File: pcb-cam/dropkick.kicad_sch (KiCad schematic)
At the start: 50 parts, among them J1 Conn_01x10, SW1 450405020524, SW2 KMR211NG_LFS, U1 SPX3819-3.3, U2 MCP73831T-2ACI/OT, U3 CAM-M8C-0, U4 ATSAMD21G18A-AUT, U5 DPS310XTSA1, U6 MPU-6050, X1 USB micro-B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

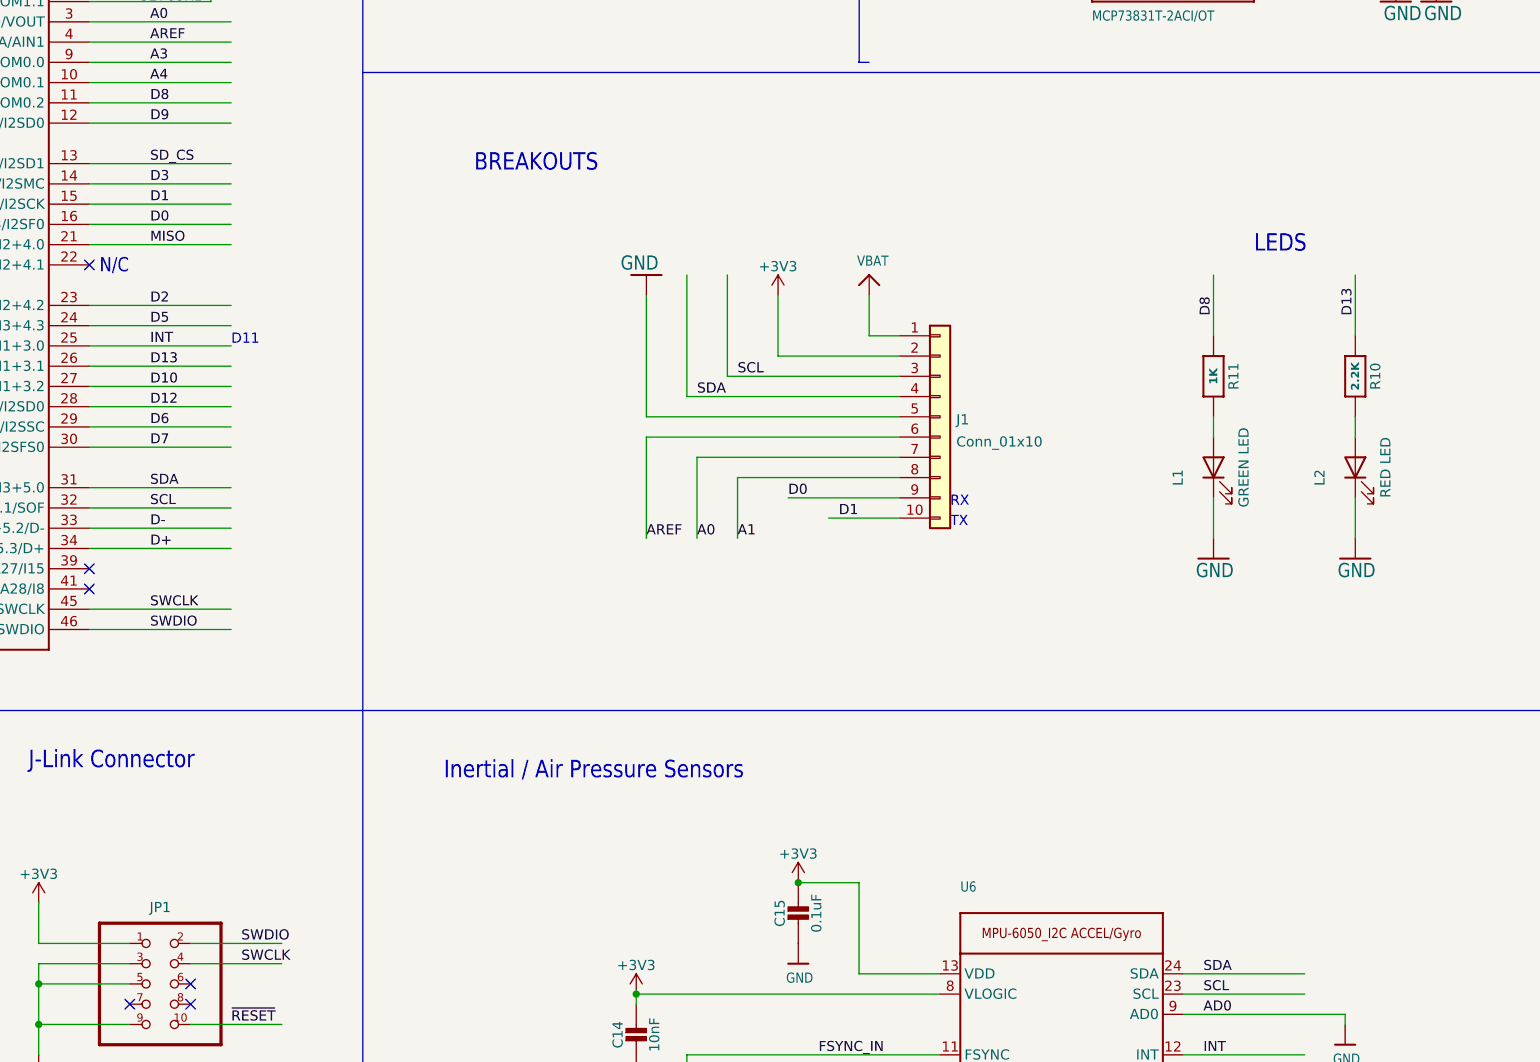
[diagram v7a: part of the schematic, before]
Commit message: Switch to 2.0mm pads and added SWDIO/SWCLK pads to flash w/o header
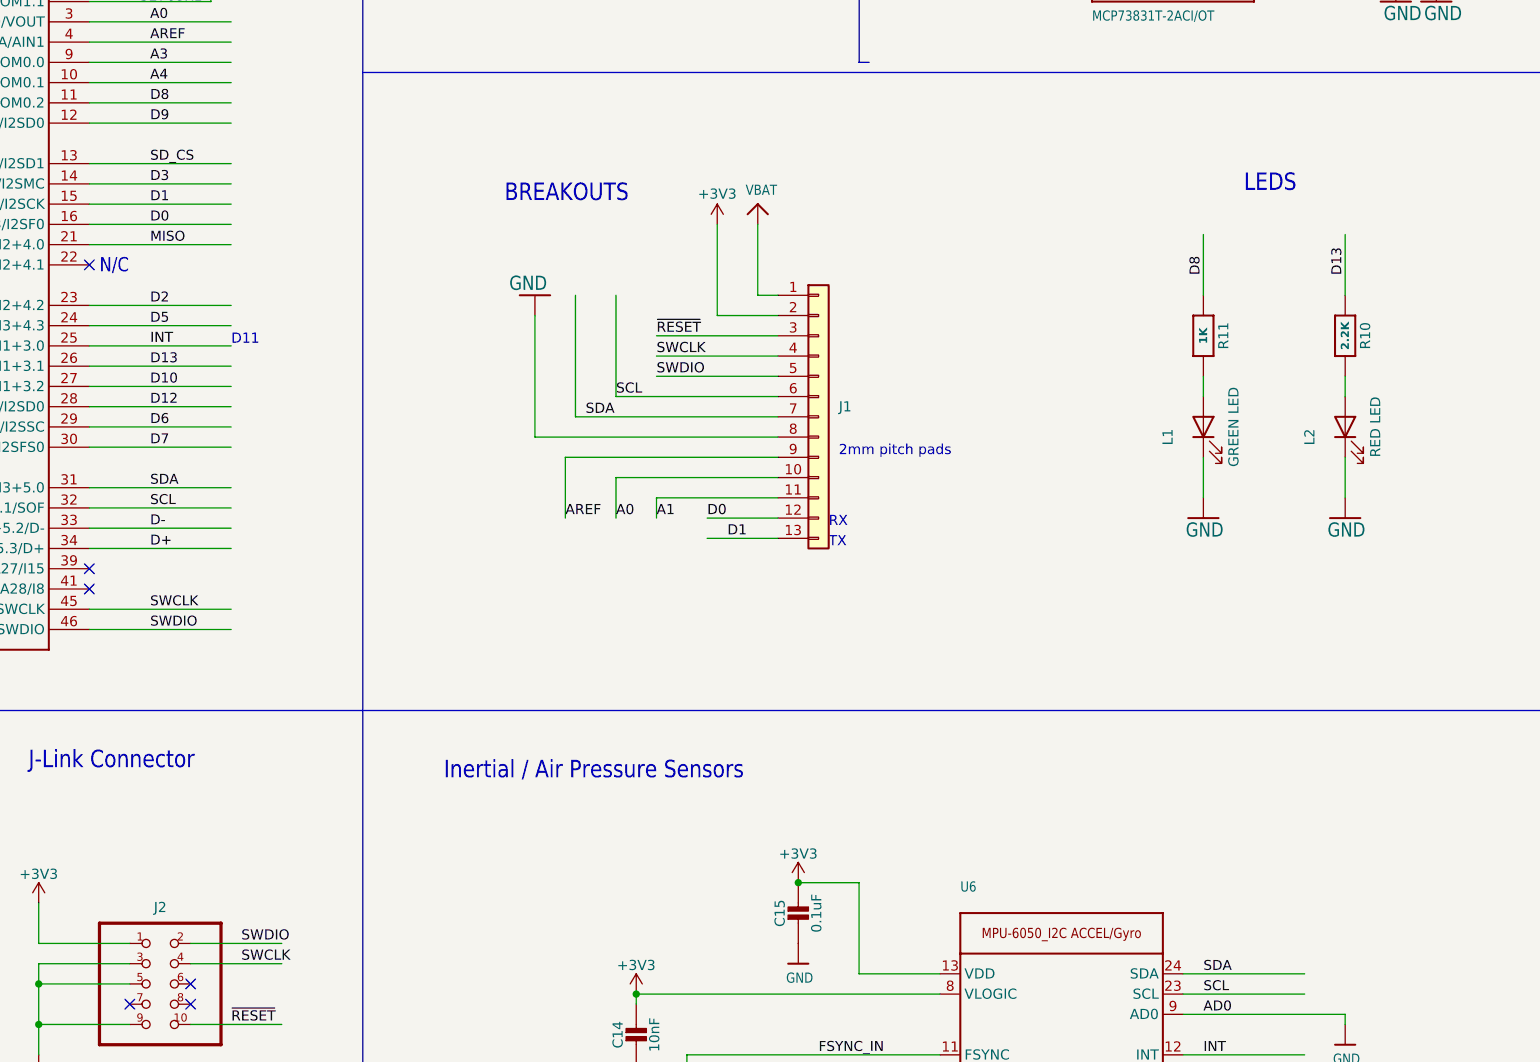
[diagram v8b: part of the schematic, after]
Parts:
- removed J1: Conn_01x10, Connector_PinSocket_2.54mm:PinSocket_1x10_P2.54mm_Vertical, symbol Connector_Generic:Conn_01x10
- added J1: Conn_01x13, Connector_PinSocket_2.00mm:PinSocket_1x13_P2.00mm_Vertical, symbol Connector_Generic:Conn_01x13
- R12, R13, R14, R4: Comments R11-R12 DNP -> (none)
- renumbered JP1 to J2
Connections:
- net +3V3: now also J1.2 (Pin_2)
- net A0: now also J1.10 (Pin_10)
- net A1: now also J1.11 (Pin_11)
- net AREF: now also J1.9 (Pin_9)
- net D0: now also J1.12 (Pin_12)
- net D1: now also J1.13 (Pin_13)
- net GND: now also J1.8 (Pin_8)
- net SCL: now also J1.6 (Pin_6)
- net SDA: now also J1.7 (Pin_7)
- net SWCLK: now also J1.4 (Pin_4)
- net SWDIO: now also J1.5 (Pin_5)
- net VBAT: now also J1.1 (Pin_1)
- net ~{RESET}: now also J1.3 (Pin_3)
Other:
- note added: "2mm pitch pads"
- title: Dropkick -> Dropkick CAM
- moved on the sheet: L1, L2, R10, R11
